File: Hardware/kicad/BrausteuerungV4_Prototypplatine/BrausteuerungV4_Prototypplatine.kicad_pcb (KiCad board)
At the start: 2 copper layers, 1 part

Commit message: added PCB
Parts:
- added Piezzo: PIEZO-MCKPI-G1410, myKiCadLib:PIEZO-MCKPI-G1410, F.Cu at (75.6, 70.9)
- added R4,7K: R_Axial_DIN0309_L9.0mm_D3.2mm_P20.32mm_Horizontal, Resistor_THT:R_Axial_DIN0309_L9.0mm_D3.2mm_P20.32mm_Horizontal, F.Cu at (85.6, 60.9)
- added Stereo3,5: EAR, myKiCadLib:Tayda_3.5mm_stereo_TRS_jack_A-853, F.Cu at (77.5, 56.8)
- added TR433MHz FS1000A: RF_Transmitter_433_MHz, myKiCadLib:RF_Transmitter_433_MHz, F.Cu at (77.4, 84.2)
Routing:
- net (no net): track 0.00 -> 158.6 mm

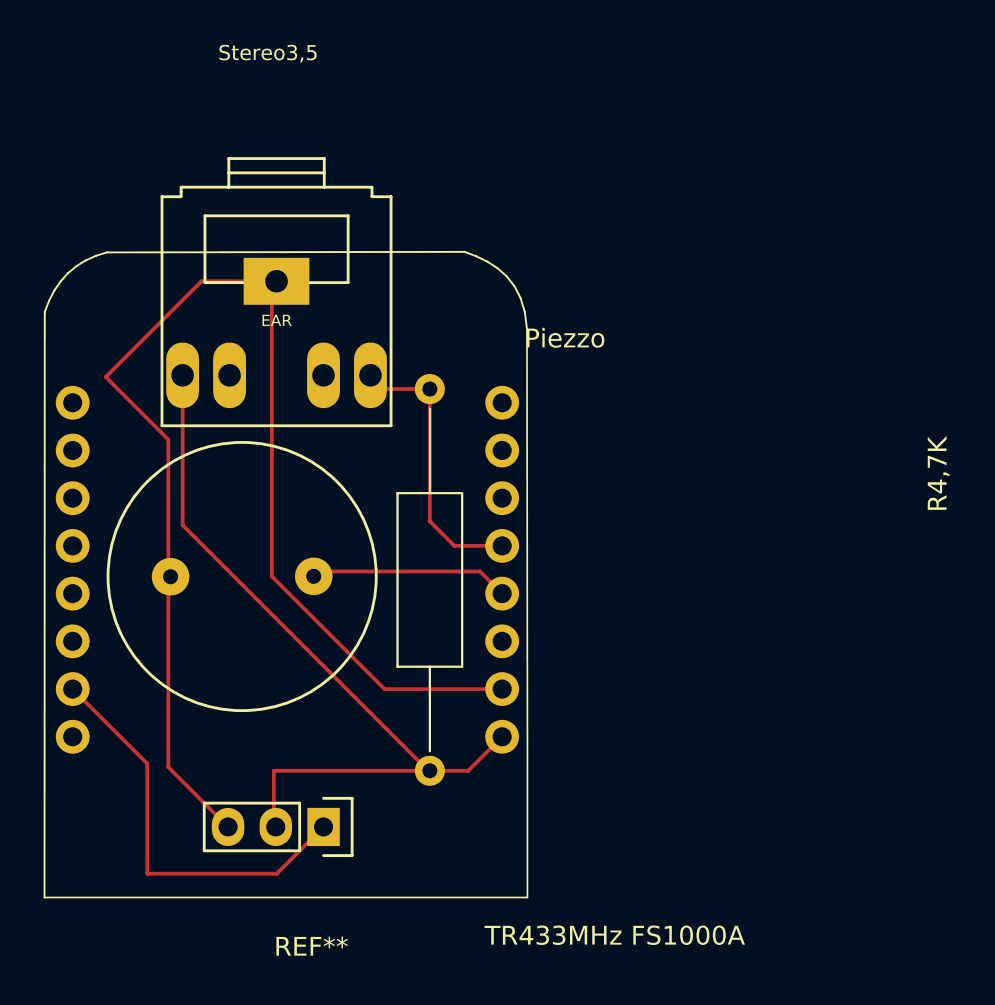
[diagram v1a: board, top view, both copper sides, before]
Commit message: gerber created to send to elecrow
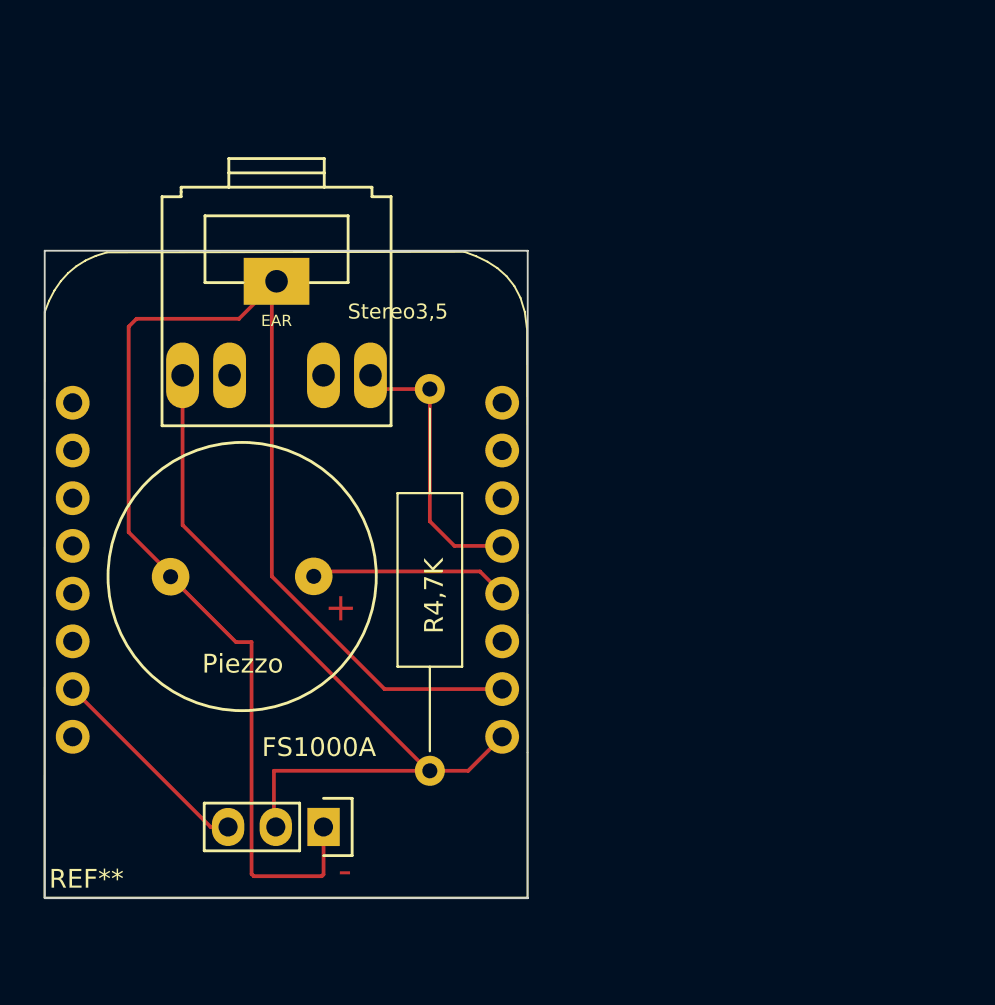
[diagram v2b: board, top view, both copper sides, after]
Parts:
- FS1000A: renamed from TR433MHz FS1000A
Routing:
- net (no net): track 158.6 -> 157.1 mm
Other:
- board outline added: 25.7 x 34.5 mm
- board text added: "+"
- board text added: "-"
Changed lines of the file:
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@@
   )
   (paper "A4")
+  (title_block
+    (title "Brausteuerung V4")
+    (company "Zwieselbrau.de")
+  )
   (layers
     (0 "F.Cu" signal)
@@
   )
   (setup
+    (stackup
+      (layer "F.SilkS" (type "Top Silk Screen"))
+      (layer "F.Paste" (type "Top Solder Paste"))
+      (layer "F.Mask" (type "Top Solder Mask") (thickness 0.01))
+      (layer "F.Cu" (type "copper") (thickness 0.035))
+      (layer "dielectric 1" (type "core") (thickness 1.51) (material "FR4") (epsilon_r 4.5) (loss_tangent 0.02))
+      (layer "B.Cu" (type "copper") (thickness 0.035))
+      (layer "B.Mask" (type "Bottom Solder Mask") (thickness 0.01))
+      (layer "B.Paste" (type "Bottom Solder Paste"))
+      (layer "B.SilkS" (type "Bottom Silk Screen"))
+      (copper_finish "None")
+      (dielectric_constraints no)
+    )
     (pad_to_mask_clearance 0)
+    (aux_axis_origin 65.06 87.9)
     (pcbplotparams
       (layerselection 0x00010fc_ffffffff)
@@
       (sketchpadsonfab false)
       (subtractmaskfromsilk false)
-      (outputformat 1)
+      (outputformat 4)
       (mirror false)
-      (drillshape 1)
+      (drillshape 0)
       (scaleselection 1)
-      (outputdirectory "")
+      (outputdirectory "./")
     )
   )
@@
     (tags "Resistor Axial_DIN0309 series Axial Horizontal pin pitch 20.32mm 0.5W = 1/2W length 9mm diameter 3.2mm")
     (attr through_hole)
-    (fp_text reference "R4,7K" (at 4.55 -27.04 90) (layer "F.SilkS")
-      (effects (font (size 1 1) (thickness 0.15)))
-    )
-    (fp_text value "R_Axial_DIN0309_L9.0mm_D3.2mm_P20.32mm_Horizontal" (at 10.23 -29.56 90) (layer "F.Fab")
-      (effects (font (size 1 1) (thickness 0.15)))
-    )
-    (fp_text user "${REFERENCE}" (at 10.45 -27.11 90) (layer "F.Fab")
+    (fp_text reference "R4,7K" (at 11.01 -0.23 90) (layer "F.SilkS")
+      (effects (font (size 1 1) (thickness 0.15)))
+    )
+    (fp_text value "R_Axial_DIN0309_L9.0mm_D3.2mm_P20.32mm_Horizontal" (at 8.49 -7.42 90) (layer "F.Fab")
       (effects (font (size 1 1) (thickness 0.15)))
     )
@@
     (at 75.63 70.88 180)
     (attr through_hole)
-    (fp_text reference "Piezzo" (at -17.19 12.66) (layer "F.SilkS")
-      (effects (font (size 1 1) (thickness 0.15)))
-    )
-    (fp_text value "PIEZO-MCKPI-G1410" (at -23.16 10.86) (layer "F.Fab")
+    (fp_text reference "Piezzo" (at -0.03 -4.65) (layer "F.SilkS")
+      (effects (font (size 1 1) (thickness 0.15)))
+    )
+    (fp_text value "PIEZO-MCKPI-G1410" (at -0.74 2.96) (layer "F.Fab")
       (effects (font (size 1 1) (thickness 0.15)))
     )
@@
     (at 78.04 71.79)
     (attr through_hole)
-    (fp_text reference "REF**" (at 1.27 18.81) (layer "F.SilkS")
-      (effects (font (size 1 1) (thickness 0.15)))
-    )
-    (fp_text value "D1_mini_board" (at 1.27 -19.05) (layer "F.Fab")
+    (fp_text reference "REF**" (at -10.7 15.19) (layer "F.SilkS")
+      (effects (font (size 1 1) (thickness 0.15)))
+    )
+    (fp_text value "D1_mini_board" (at -18.62 -16.58) (layer "F.Fab")
       (effects (font (size 1 1) (thickness 0.15)))
     )
@@
     (at 77.46 56.76)
     (attr through_hole)
-    (fp_text reference "Stereo3,5" (at -0.44 -13.74) (layer "F.SilkS")
+    (fp_text reference "Stereo3,5" (at 6.46 0.02) (layer "F.SilkS")
       (effects (font (size 0.8 0.8) (thickness 0.15)))
     )
@@
     (at 77.42 84.21 180)
     (attr through_hole)
-    (fp_text reference "TR433MHz FS1000A" (at -18.05 -5.8005) (layer "F.SilkS")
-      (effects (font (size 1 1) (thickness 0.15)))
-    )
-    (fp_text value "RF_Transmitter_433_MHz" (at -23.66 -7.9605) (layer "F.Fab")
+    (fp_text reference "FS1000A" (at -2.3 4.24) (layer "F.SilkS")
+      (effects (font (size 1 1) (thickness 0.15)))
+    )
+    (fp_text value "RF_Transmitter_433_MHz" (at 1.42 -8.76) (layer "F.Fab")
       (effects (font (size 1 1) (thickness 0.15)))
     )
@@
     (pad "3" thru_hole oval locked (at 2.54 0 270) (size 2.032 1.7272) (drill 1.016) (layers *.Cu *.Mask "F.SilkS"))
   )
+  (gr_rect (start 65.12 53.54) (end 90.83 88) (layer "Edge.Cuts") (width 0.1) (fill none))
+  (gr_text "+" (at 80.88 72.52) (layer "F.Cu")
+    (effects (font (size 1.5 1.5) (thickness 0.3)))
+  )
+  (gr_text "-" (at 81.1 86.52) (layer "F.Cu")
+    (effects (font (size 1.5 1.5) (thickness 0.3)))
+  )
+  (dimension (type aligned) (layer "F.Cu")
+    (pts (xy 65.08 87.88) (xy 90.8 87.88))
+    (height 9.2)
+    (gr_text "25,7200 mm" (at 77.94 95.28) (layer "F.Cu")
+      (effects (font (size 1.5 1.5) (thickness 0.3)))
+    )
+    (format (units 3) (units_format 1) (precision 4))
+    (style (thickness 0.2) (arrow_length 1.27) (text_position_mode 0) (extension_height 0.58642) (extension_offset 0.5) keep_text_aligned)
+  )
+  (dimension (type aligned) (layer "F.Cu")
+    (pts (xy 90.75 87.89) (xy 90.75 53.63))
+    (height 7.55)
+    (gr_text "34,2600 mm" (at 96.5 70.76 90) (layer "F.Cu")
+      (effects (font (size 1.5 1.5) (thickness 0.3)))
+    )
+    (format (units 3) (units_format 1) (precision 4))
+    (style (thickness 0.2) (arrow_length 1.27) (text_position_mode 0) (extension_height 0.58642) (extension_offset 0.5) keep_text_aligned)
+  )
   (segment (start 83.19 60.9) (end 82.46 60.17) (width 0.2) (layer "F.Cu") (net 0))
   (segment (start 77.32 84.11) (end 77.32 81.22) (width 0.2) (layer "F.Cu") (net 0))
   (segment (start 77.46 55.164) (end 77.21 55.414) (width 0.2) (layer "F.Cu") (net 0))
-  (segment (start 71.7 63.59) (end 68.37 60.26) (width 0.2) (layer "F.Cu") (net 0))
-  (segment (start 71.7 70.63) (end 71.7 63.59) (width 0.2) (layer "F.Cu") (net 0))
-  (segment (start 73.466 55.164) (end 77.46 55.164) (width 0.2) (layer "F.Cu") (net 0))
+  (segment (start 74.88 84.21) (end 73.95 84.21) (width 0.2) (layer "F.Cu") (net 0))
   (segment (start 83.21 76.87) (end 89.47 76.87) (width 0.2) (layer "F.Cu") (net 0))
   (segment (start 77.21 55.414) (end 77.21 70.87) (width 0.2) (layer "F.Cu") (net 0))
+  (segment (start 73.95 84.21) (end 66.61 76.87) (width 0.2) (layer "F.Cu") (net 0))
   (segment (start 85.62 60.9) (end 83.19 60.9) (width 0.2) (layer "F.Cu") (net 0))
+  (segment (start 79.96 86.74) (end 79.87 86.83) (width 0.2) (layer "F.Cu") (net 0))
   (segment (start 89.47 79.41) (end 87.66 81.22) (width 0.2) (layer "F.Cu") (net 0))
-  (segment (start 87.66 81.22) (end 85.62 81.22) (width 0.2) (layer "F.Cu") (net 0))
+  (segment (start 77.32 81.22) (end 87.66 81.22) (width 0.2) (layer "F.Cu") (net 0))
+  (segment (start 79.96 84.21) (end 79.96 86.74) (width 0.2) (layer "F.Cu") (net 0))
   (segment (start 85.62 67.94) (end 86.93 69.25) (width 0.2) (layer "F.Cu") (net 0))
   (segment (start 79.32 70.61) (end 88.29 70.61) (width 0.2) (layer "F.Cu") (net 0))
-  (segment (start 77.47 86.7) (end 70.6 86.7) (width 0.2) (layer "F.Cu") (net 0))
-  (segment (start 70.58 80.84) (end 66.61 76.87) (width 0.2) (layer "F.Cu") (net 0))
-  (segment (start 79.96 84.21) (end 77.47 86.7) (width 0.2) (layer "F.Cu") (net 0))
-  (segment (start 85.62 81.22) (end 85.54 81.22) (width 0.2) (layer "F.Cu") (net 0))
-  (segment (start 68.37 60.26) (end 73.466 55.164) (width 0.2) (layer "F.Cu") (net 0))
+  (segment (start 69.59 57.58) (end 70.01 57.16) (width 0.2) (layer "F.Cu") (net 0))
+  (segment (start 76.13 74.37) (end 75.3 74.37) (width 0.2) (layer "F.Cu") (net 0))
+  (segment (start 70.01 57.16) (end 75.464 57.16) (width 0.2) (layer "F.Cu") (net 0))
+  (segment (start 79.87 86.83) (end 76.25 86.83) (width 0.2) (layer "F.Cu") (net 0))
   (segment (start 88.29 70.61) (end 89.47 71.79) (width 0.2) (layer "F.Cu") (net 0))
+  (segment (start 71.7 70.63) (end 69.59 68.52) (width 0.2) (layer "F.Cu") (net 0))
   (segment (start 77.21 70.87) (end 83.21 76.87) (width 0.2) (layer "F.Cu") (net 0))
-  (segment (start 70.6 86.7) (end 70.58 86.68) (width 0.2) (layer "F.Cu") (net 0))
-  (segment (start 89.47 79.72) (end 89.47 79.41) (width 0.2) (layer "F.Cu") (net 0))
-  (segment (start 77.32 81.22) (end 85.62 81.22) (width 0.2) (layer "F.Cu") (net 0))
-  (segment (start 71.7 81.03) (end 74.88 84.21) (width 0.2) (layer "F.Cu") (net 0))
-  (segment (start 71.7 70.63) (end 71.7 81.03) (width 0.2) (layer "F.Cu") (net 0))
   (segment (start 86.93 69.25) (end 89.47 69.25) (width 0.2) (layer "F.Cu") (net 0))
   (segment (start 77.42 84.21) (end 77.32 84.11) (width 0.2) (layer "F.Cu") (net 0))
+  (segment (start 76.13 86.71) (end 76.13 74.37) (width 0.2) (layer "F.Cu") (net 0))
   (segment (start 85.54 81.22) (end 72.46 68.14) (width 0.2) (layer "F.Cu") (net 0))
-  (segment (start 70.58 86.68) (end 70.58 80.84) (width 0.2) (layer "F.Cu") (net 0))
+  (segment (start 75.464 57.16) (end 77.46 55.164) (width 0.2) (layer "F.Cu") (net 0))
+  (segment (start 69.59 68.52) (end 69.59 57.58) (width 0.2) (layer "F.Cu") (net 0))
   (segment (start 72.46 68.14) (end 72.46 60.17) (width 0.2) (layer "F.Cu") (net 0))
   (segment (start 85.62 60.9) (end 85.62 67.94) (width 0.2) (layer "F.Cu") (net 0))
+  (segment (start 75.3 74.37) (end 71.82 70.89) (width 0.2) (layer "F.Cu") (net 0))
+  (segment (start 76.25 86.83) (end 76.13 86.71) (width 0.2) (layer "F.Cu") (net 0))
 )
